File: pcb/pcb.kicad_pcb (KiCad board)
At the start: 2 copper layers, 73 x 55.9 mm, 19 parts, among them Q1 2N3906

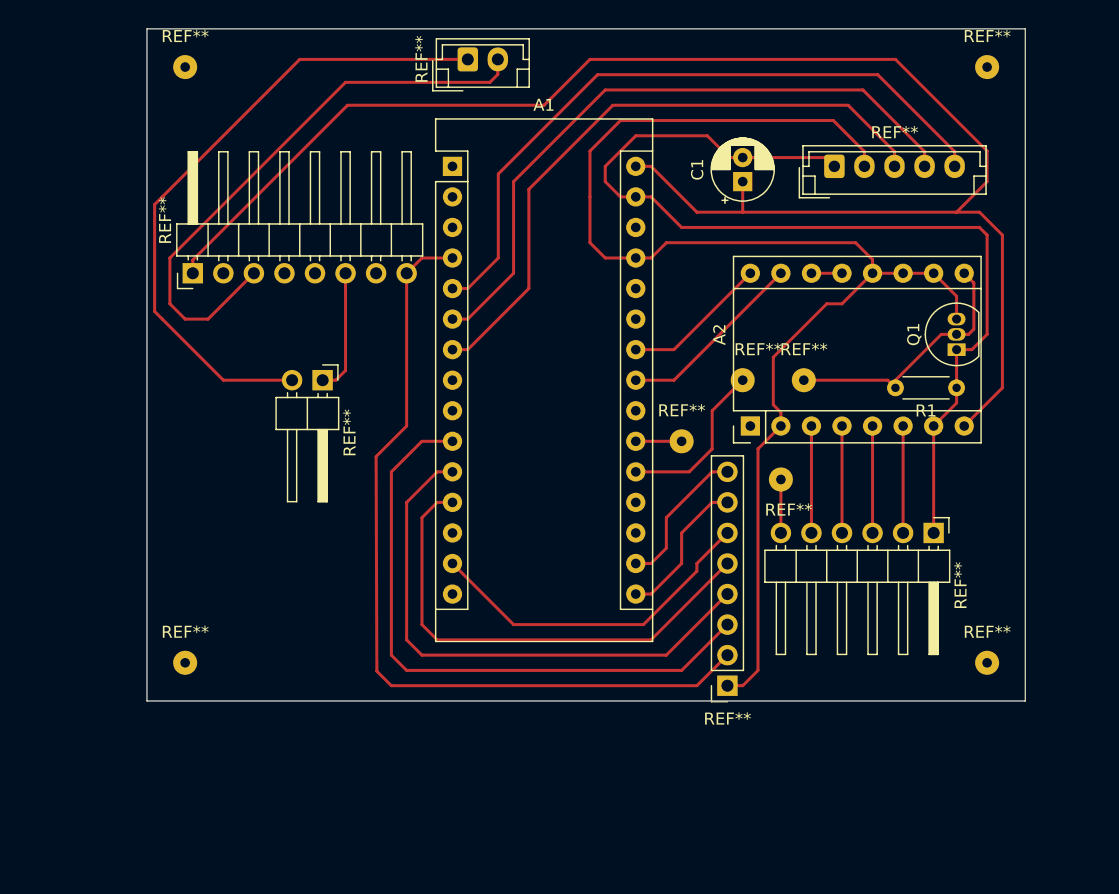
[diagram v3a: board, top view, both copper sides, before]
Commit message: update cad structure, pcb mounting holes, display mounting holes
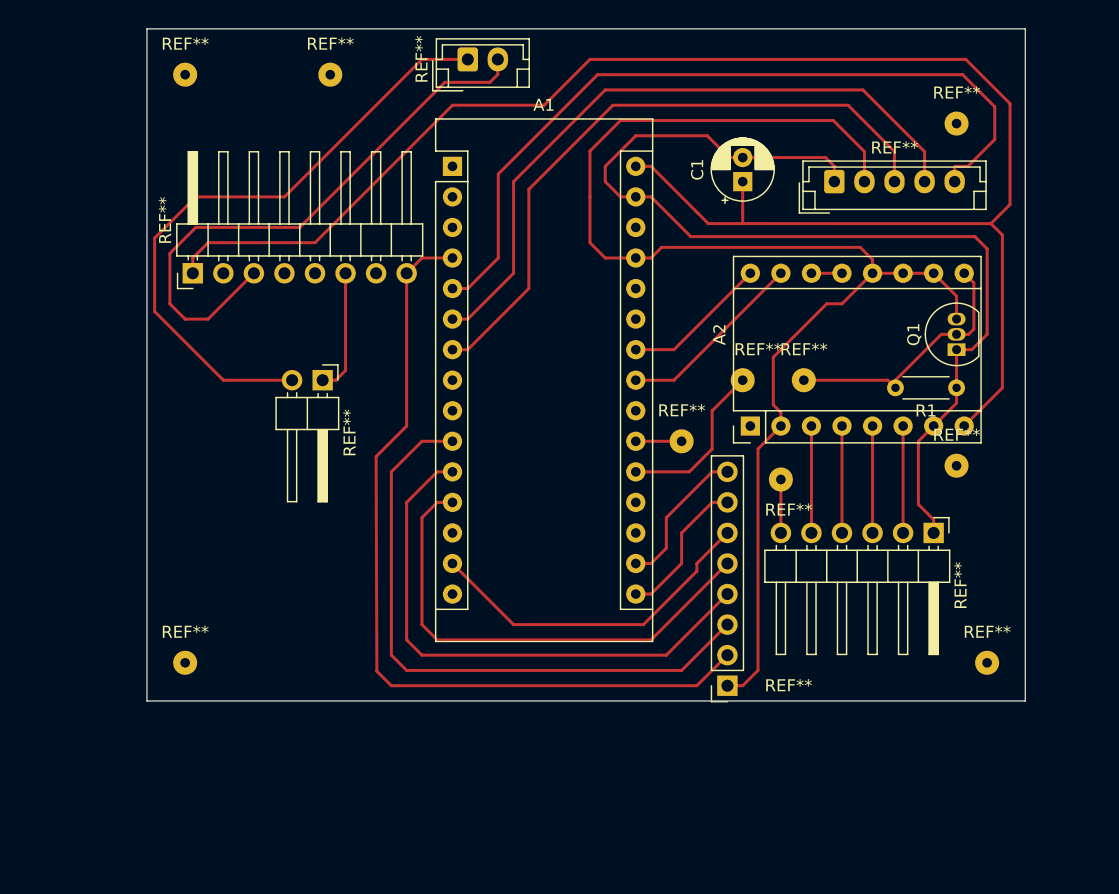
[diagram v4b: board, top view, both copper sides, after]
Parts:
- added REF**: ., Connector_Wire:SolderWirePad_1x01_Drill0.8mm, F.Cu at (71.1, 43.2)
- added REF**: ., Connector_Wire:SolderWirePad_1x01_Drill0.8mm, F.Cu at (123.2, 75.7)
- moved REF** 5.34 mm to (123.2, 47.2)
- moved REF** 1.27 mm to (113.0, 52.1)
- moved REF** 0.63 mm to (59.1, 43.2)
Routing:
- net encoder_dt: track 57.1 -> 65.9 mm
- net ardu_vcc: track 135.9 -> 141.7 mm
- net ardu_gnd: track 83.4 -> 85.0 mm
- net (no net): track 111.8 -> 110.4 mm
- net encoder_sw: track 52.8 -> 54.1 mm
- net encoder_clk: track 55.0 -> 56.2 mm
- net ardu_5v: track 37.9 -> 39.2 mm

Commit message: update
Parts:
- moved REF** 2.54 mm to (125.7, 89.5)
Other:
- outline, holes or cut-outs redrawn
